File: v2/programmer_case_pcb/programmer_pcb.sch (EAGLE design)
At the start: 17 parts, among them J1 1X2-3.5MM, SW1 SPST_TACT-EVQQ2

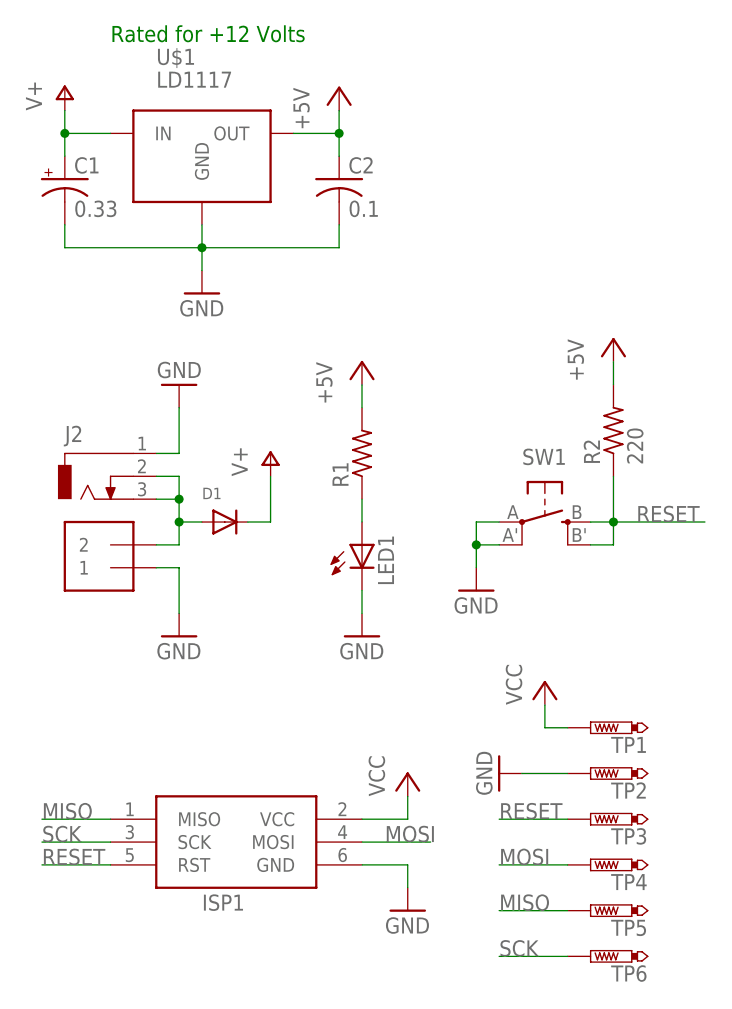
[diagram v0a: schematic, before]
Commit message: start populating some of the components
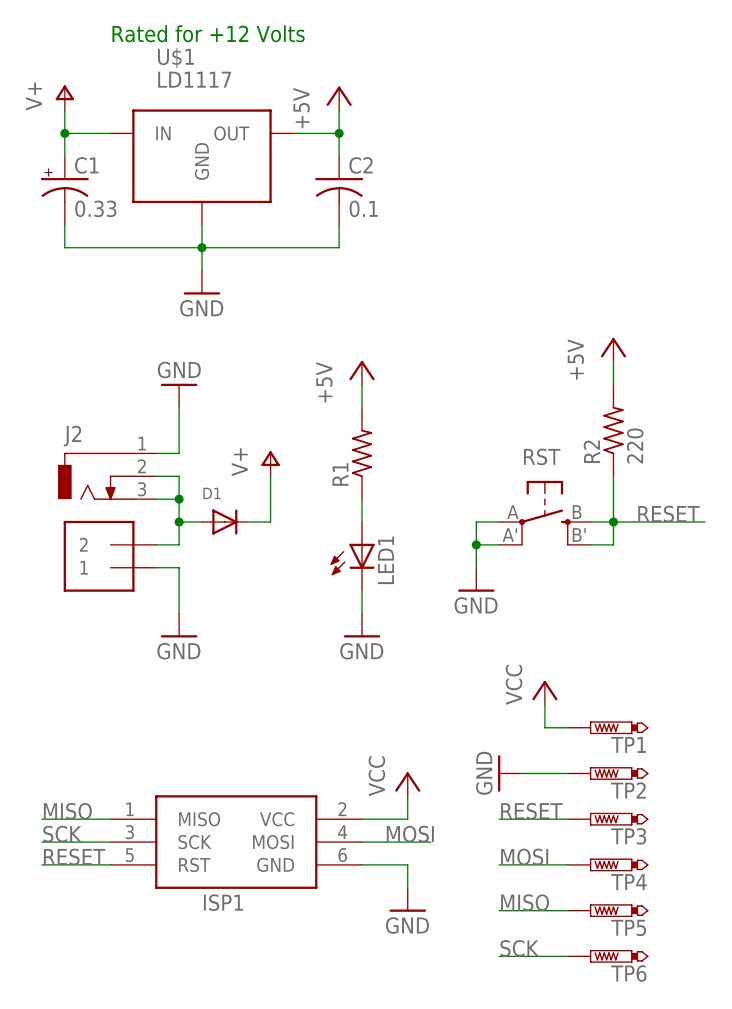
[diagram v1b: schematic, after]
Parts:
- renumbered SW1 to RST
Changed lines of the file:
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@@
 <part name="P+5" library="supply1" library_urn="urn:adsk.eagle:library:371" deviceset="+5V" device=""/>
 <part name="GND4" library="supply1" library_urn="urn:adsk.eagle:library:371" deviceset="GND" device=""/>
-<part name="SW1" library="adafruit" library_urn="urn:adsk.eagle:library:420" deviceset="SPST_TACT" device="-EVQQ2" package3d_urn="urn:adsk.eagle:package:6240643/1"/>
+<part name="RST" library="adafruit" library_urn="urn:adsk.eagle:library:420" deviceset="SPST_TACT" device="-EVQQ2" package3d_urn="urn:adsk.eagle:package:6240643/1"/>
 <part name="GND5" library="supply1" library_urn="urn:adsk.eagle:library:371" deviceset="GND" device=""/>
 <part name="R2" library="adafruit" deviceset="R-US_" device="R0805" package3d_urn="urn:adsk.eagle:package:6240566/1" value="220"/>
@@
 <attribute name="VALUE" x="45.72" y="68.58" size="1.778" layer="96"/>
 </instance>
-<instance part="SW1" gate="G$1" x="68.58" y="83.82" smashed="yes" rot="R270">
+<instance part="RST" gate="G$1" x="68.58" y="83.82" smashed="yes" rot="R270">
 <attribute name="NAME" x="66.04" y="90.17" size="1.778" layer="95"/>
 </instance>
@@
 <pinref part="GND5" gate="1" pin="GND"/>
 <wire x1="60.96" y1="78.74" x2="60.96" y2="81.28" width="0.1524" layer="91"/>
-<pinref part="SW1" gate="G$1" pin="P1"/>
+<pinref part="RST" gate="G$1" pin="P1"/>
 <wire x1="60.96" y1="81.28" x2="63.5" y2="81.28" width="0.1524" layer="91"/>
 <wire x1="60.96" y1="81.28" x2="60.96" y2="83.82" width="0.1524" layer="91"/>
 <junction x="60.96" y="81.28"/>
-<pinref part="SW1" gate="G$1" pin="P"/>
+<pinref part="RST" gate="G$1" pin="P"/>
 <wire x1="60.96" y1="83.82" x2="63.5" y2="83.82" width="0.1524" layer="91"/>
 </segment>
@@
 </segment>
 <segment>
-<pinref part="SW1" gate="G$1" pin="S"/>
+<pinref part="RST" gate="G$1" pin="S"/>
 <pinref part="R2" gate="G$1" pin="1"/>
 <wire x1="73.66" y1="83.82" x2="76.2" y2="83.82" width="0.1524" layer="91"/>
 <wire x1="76.2" y1="83.82" x2="76.2" y2="88.9" width="0.1524" layer="91"/>
-<pinref part="SW1" gate="G$1" pin="S1"/>
+<pinref part="RST" gate="G$1" pin="S1"/>
 <wire x1="73.66" y1="81.28" x2="76.2" y2="81.28" width="0.1524" layer="91"/>
 <wire x1="76.2" y1="81.28" x2="76.2" y2="83.82" width="0.1524" layer="91"/>
